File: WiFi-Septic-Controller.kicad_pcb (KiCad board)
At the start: 2 copper layers, 80 x 90 mm, 104 parts, among them J1 Screw_Terminal_01x02, J2 Screw_Terminal_01x02, J3 Screw_Terminal_01x03, J4 Screw_Terminal_01x06, J5 USB_B_Micro, J6 GWT-C1627A-RGB, J7 Cortex Debug, J8 Screw_Terminal_01x03, Q1 2N7002, Q2 2N7002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

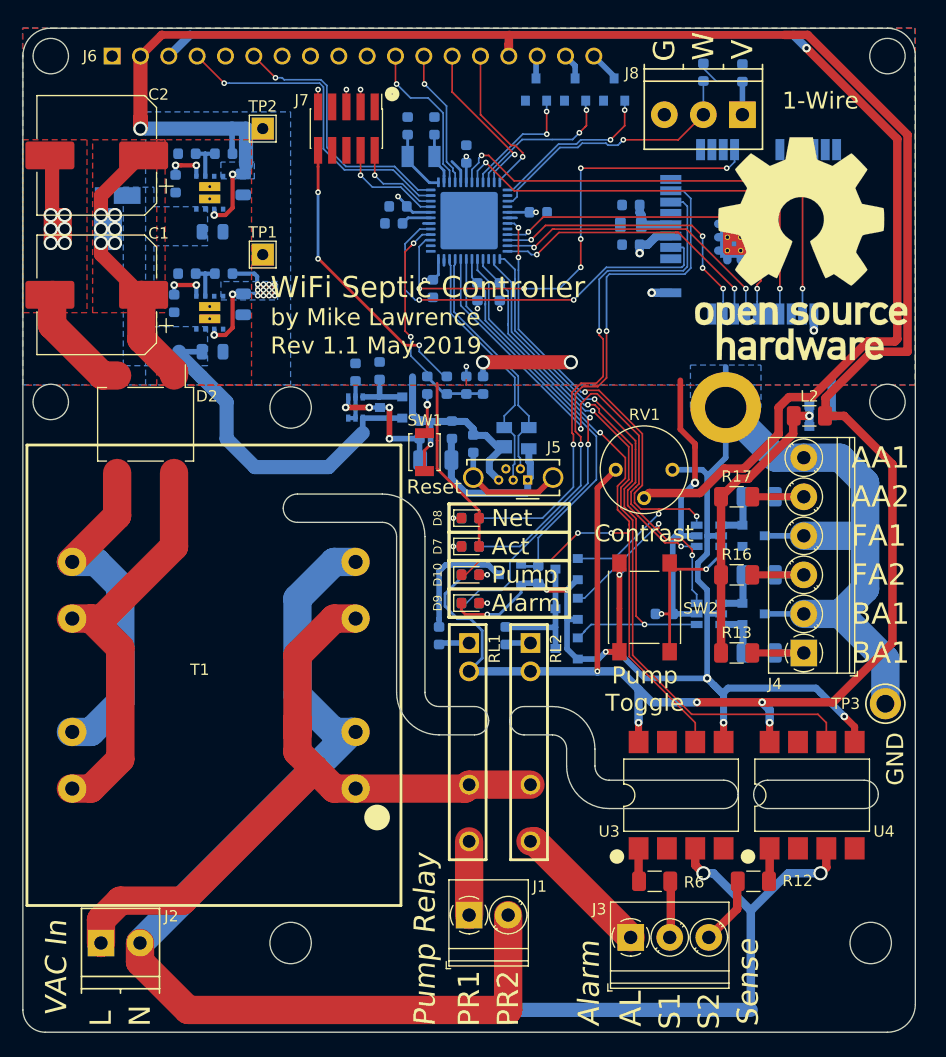
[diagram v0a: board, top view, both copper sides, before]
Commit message: Cleanup BOM. VCC now +3V3.
Add KiBoM support.
Cleanup part information in schematic.
Added power pins to schematic on multi-unit gates.
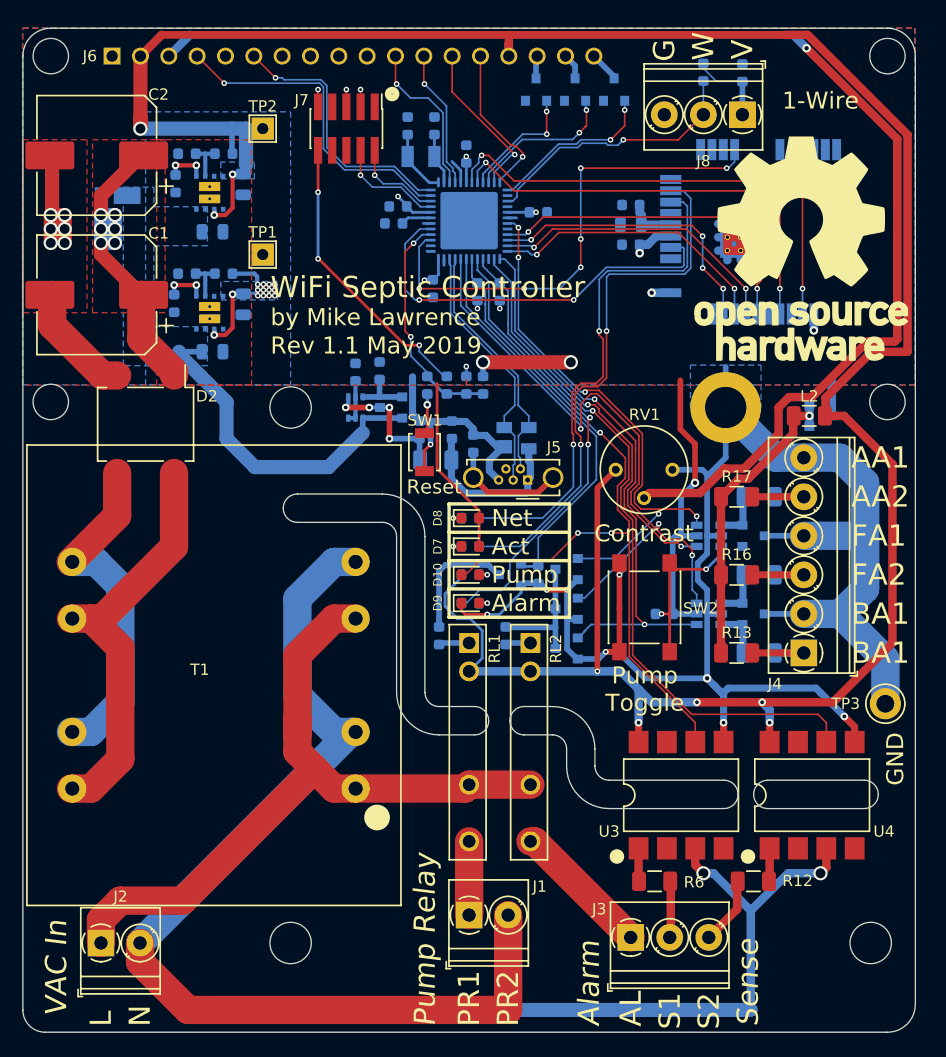
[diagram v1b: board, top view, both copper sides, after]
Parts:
- C4, C9: value 3.3nF -> 3300pF
- C6, C7: value 1nF -> 1000pF
- J2: footprint TerminalBlock_Phoenix:TerminalBlock_Phoenix_PT-3.5mm_2pol -> TerminalBlock_Phoenix:TerminalBlock_Phoenix_PT-1,5-2-3.5-H_1x02_P3.50mm_Horizontal
- J8: footprint TerminalBlock_Phoenix:TerminalBlock_Phoenix_PT-3.5mm_3pol -> TerminalBlock_Phoenix:TerminalBlock_Phoenix_PT-1,5-3-3.5-H_1x03_P3.50mm_Horizontal
- L1, L2: value 1k@1MHz -> 1k@100MHz
- L3: value 470@1MHz -> 470@100MHz
- R19, R20, R21: value 130 -> 130R
- R23: value 39 -> 39R
- R25: value 330 -> 330R
- R28, R29: value 698 -> 698R
- R4: value 169 -> 169R
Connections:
- net VCC renamed +3V3
